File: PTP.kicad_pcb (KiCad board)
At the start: 2 copper layers, 41 x 36 mm, 33 parts, among them CON1 USB MiniB, J1 Conn_01x04_Pin, SW1 SW_SPDT, U1 STM32F103C8T6, U2 USBLC6-2SC6, U3 SPX3819M5-L-3-3, Y1 16MHz

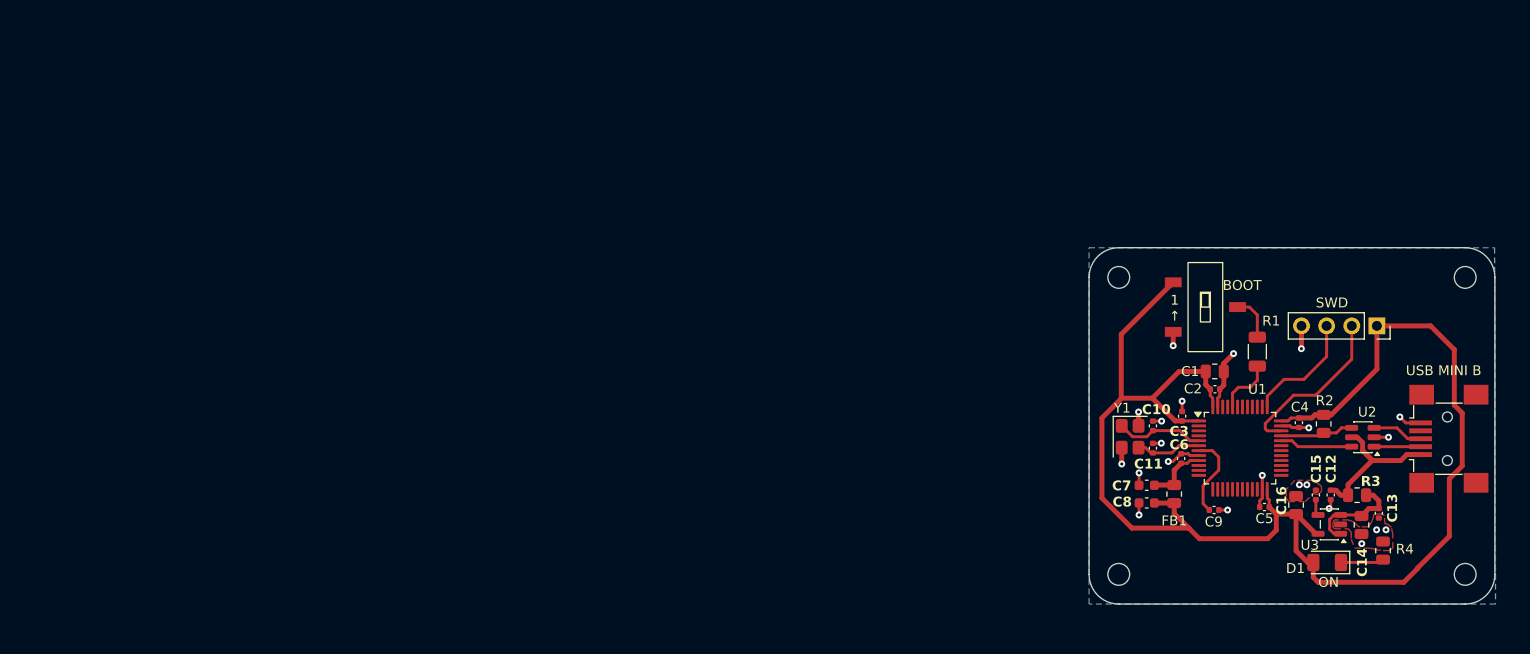
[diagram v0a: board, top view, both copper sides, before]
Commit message: v1.1 PTP project - full GPIO breakout, STDC14 port for stlinkv3minie programming
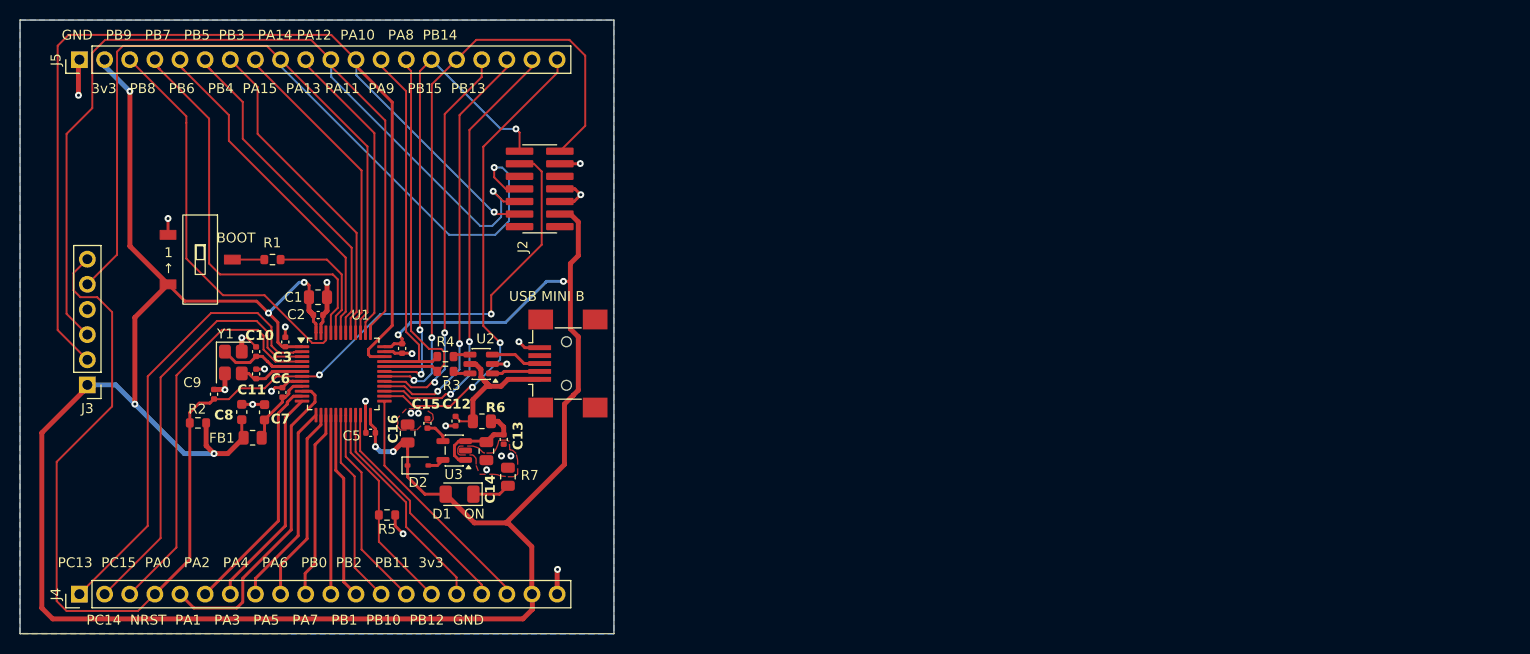
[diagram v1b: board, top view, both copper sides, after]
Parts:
- removed H1, H2, H3, H4: MountingHole, MountingHole:MountingHole_2.2mm_M2
- removed the J1 at (216.1, 104.9)
- added D2: RB161VA-20TR, Diode_SMD:D_SOD-323, F.Cu at (119.2, 119.0)
- added J2: JTAG ST_STDC14, PTP_Projekt:FTSH-107-01-L-DV-K, F.Cu at (129.8, 96.2)
- added J3: SWDBG, Connector_PinHeader_2.54mm:PinHeader_1x06_P2.54mm_Vertical, F.Cu at (85.8, 110.9)
- added J4: Left, Connector_PinHeader_2.54mm:PinHeader_1x20_P2.54mm_Vertical, F.Cu at (85.0, 132.0)
- added J5: Right, Connector_PinHeader_2.54mm:PinHeader_1x20_P2.54mm_Vertical, F.Cu at (85.0, 78.0)
- added R3: 22, Resistor_SMD:R_0603_1608Metric, F.Cu at (122.0, 109.5)
- added R4: 22, Resistor_SMD:R_0603_1608Metric, F.Cu at (122.0, 108.0)
- added R5: 10k, Resistor_SMD:R_0603_1608Metric, F.Cu at (116.1, 124.0)
- R1: footprint Resistor_SMD:R_1206_3216Metric -> Resistor_SMD:R_0603_1608Metric
- R2: value 1k5 -> 10k; footprint Resistor_SMD:R_0805_2012Metric -> Resistor_SMD:R_0603_1608Metric
- moved R2 113.7 mm to (97.0, 114.7), turned to 0 degrees
- moved C9 101.7 mm to (98.6, 111.8), turned to -90 degrees
- moved SW1 101.7 mm to (94.0, 105.7)
- moved R1 99.9 mm to (104.5, 98.2), turned to 0 degrees
- moved FB1 93.3 mm to (102.5, 116.2), turned to 180 degrees
- moved C8 91.9 mm to (101.4, 113.6), turned to 90 degrees
- moved C6 91.0 mm to (105.5, 111.6)
- moved C3 90.9 mm to (105.8, 106.5)
- moved Y1 90.9 mm to (100.5, 108.6)
- moved C1 90.9 mm to (109.1, 102.0)
- moved C10 90.9 mm to (102.8, 107.5)
- moved C11 90.9 mm to (102.8, 109.8)
- moved C2 90.9 mm to (109.1, 103.8)
- moved C4 90.9 mm to (117.6, 107.2)
- moved U1 90.9 mm to (111.7, 109.8)
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- renumbered CON1 to J1, R3 to R6, R4 to R7
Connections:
- R2 pad 1: +3V3 -> /NRST
- R2 pad 2: /USB_D+ -> +3V3
- SW1 pad 1: +3V3 -> GND
- SW1 pad 3: GND -> +3V3
- U1 pad 10: unconnected-(U1-PA0-Pad10) -> /PA0
- U1 pad 11: unconnected-(U1-PA1-Pad11) -> /PA1
- U1 pad 12: unconnected-(U1-PA2-Pad12) -> /PA2
- U1 pad 13: unconnected-(U1-PA3-Pad13) -> /PA3
- U1 pad 14: unconnected-(U1-PA4-Pad14) -> /PA4
- U1 pad 15: unconnected-(U1-PA5-Pad15) -> /PA5
- U1 pad 16: unconnected-(U1-PA6-Pad16) -> /PA6
- U1 pad 17: unconnected-(U1-PA7-Pad17) -> /PA7
- U1 pad 18: unconnected-(U1-PB0-Pad18) -> /PB0
- U1 pad 19: unconnected-(U1-PB1-Pad19) -> /PB1
- U1 pad 2: unconnected-(U1-PC13-Pad2) -> /PC13
- U1 pad 20: unconnected-(U1-PB2-Pad20) -> /PB2
- U1 pad 21: unconnected-(U1-PB10-Pad21) -> /PB10
- U1 pad 22: unconnected-(U1-PB11-Pad22) -> /PB11
- U1 pad 25: unconnected-(U1-PB12-Pad25) -> /PB12
- U1 pad 26: unconnected-(U1-PB13-Pad26) -> /PB13
- U1 pad 27: unconnected-(U1-PB14-Pad27) -> /PB14
- U1 pad 28: unconnected-(U1-PB15-Pad28) -> /PB15
- U1 pad 29: unconnected-(U1-PA8-Pad29) -> /PA8
- U1 pad 3: unconnected-(U1-PC14-Pad3) -> /PC14
- U1 pad 30: unconnected-(U1-PA9-Pad30) -> /USART1_TX
- U1 pad 31: unconnected-(U1-PA10-Pad31) -> /USART1_RX
- U1 pad 38: unconnected-(U1-PA15-Pad38) -> /PA15
- U1 pad 39: unconnected-(U1-PB3-Pad39) -> /PB3(SWO)
- U1 pad 4: unconnected-(U1-PC15-Pad4) -> /PC15
- U1 pad 40: unconnected-(U1-PB4-Pad40) -> /PB4
- U1 pad 41: unconnected-(U1-PB5-Pad41) -> /PB5
- U1 pad 42: unconnected-(U1-PB6-Pad42) -> /PB6
- U1 pad 43: unconnected-(U1-PB7-Pad43) -> /PB7
- U1 pad 45: unconnected-(U1-PB8-Pad45) -> /PB8
- U1 pad 46: unconnected-(U1-PB9-Pad46) -> /PB9
- U2 pad 4: /USB_D+ -> /D_R+
- U2 pad 6: /USB_D- -> /D_R-
- U3 pad 5: +3V3 -> /OUT
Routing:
- net /NRST: track 8.55 -> 124.8 mm, vias 0 -> 2
- net /PB3(SWO): track 0.00 -> 114.8 mm, vias 0 -> 1
- net +3V3: track 146.4 -> 258.3 mm, vias 0 -> 9
- net /SWCLK: track 11.8 -> 118.6 mm, vias 0 -> 1
- net /SWDIO: track 17.0 -> 122.1 mm, vias 0 -> 1
- net /USART1_TX: track 0.00 -> 63.2 mm, vias 0 -> 2
- net /USART1_RX: track 0.00 -> 50.2 mm, vias 0 -> 3
- net /PB13: track 0.00 -> 48.2 mm, vias 0 -> 2
- net /PC13: track 0.00 -> 45.9 mm
- net /PB14: track 0.00 -> 45.1 mm, vias 0 -> 2
- net /PC14: track 0.00 -> 43.3 mm
- net /PB8: track 0.00 -> 42.8 mm
- net /PB15: track 0.00 -> 41.6 mm, vias 0 -> 2
- net /PB9: track 0.00 -> 41.0 mm
- net /PC15: track 0.00 -> 40.8 mm
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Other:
- board size 41 x 36 mm -> 60 x 62 mm
- board text added: "3v3 PB8 PB6 PB4 PA15 PA13 PA11 PA9 PB15 PB13"
- board text added: "GND PB9 PB7 PB5 PB3 PA14 PA12 PA10 PA8 PB14"
- board text added: "PC13 PC15 PA0 PA2 PA4 PA6 PB0 PB2 PB11 3v3"
- board text added: "PC14 NRST PA1 PA3 PA5 PA7 PB1 PB10 PB12 GND"
- board text added: "V1.1 11/2025"
- board text removed: "SWD"
- board text removed: "V1 11/2025"
